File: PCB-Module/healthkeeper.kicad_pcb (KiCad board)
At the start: 2 copper layers, 85 x 76.8 mm, 28 parts, among them J1 RPI Conn, J2 24VDC-IN, J3 CTRL VALVE, J4 BAT Sense, J5 7"LCD Screen, J6 Flow Conn, J7 DpFlow Selector, Q1 IRF540NLPBF, U1 MCP4921-EP, U2 MCP6241, U3 TEN20-2411WIN, U4 MCP3208, U5 HSCSAAN001PDAA5, U6 HSCSAAN001PDAA5, U7 SDP816-125Pa

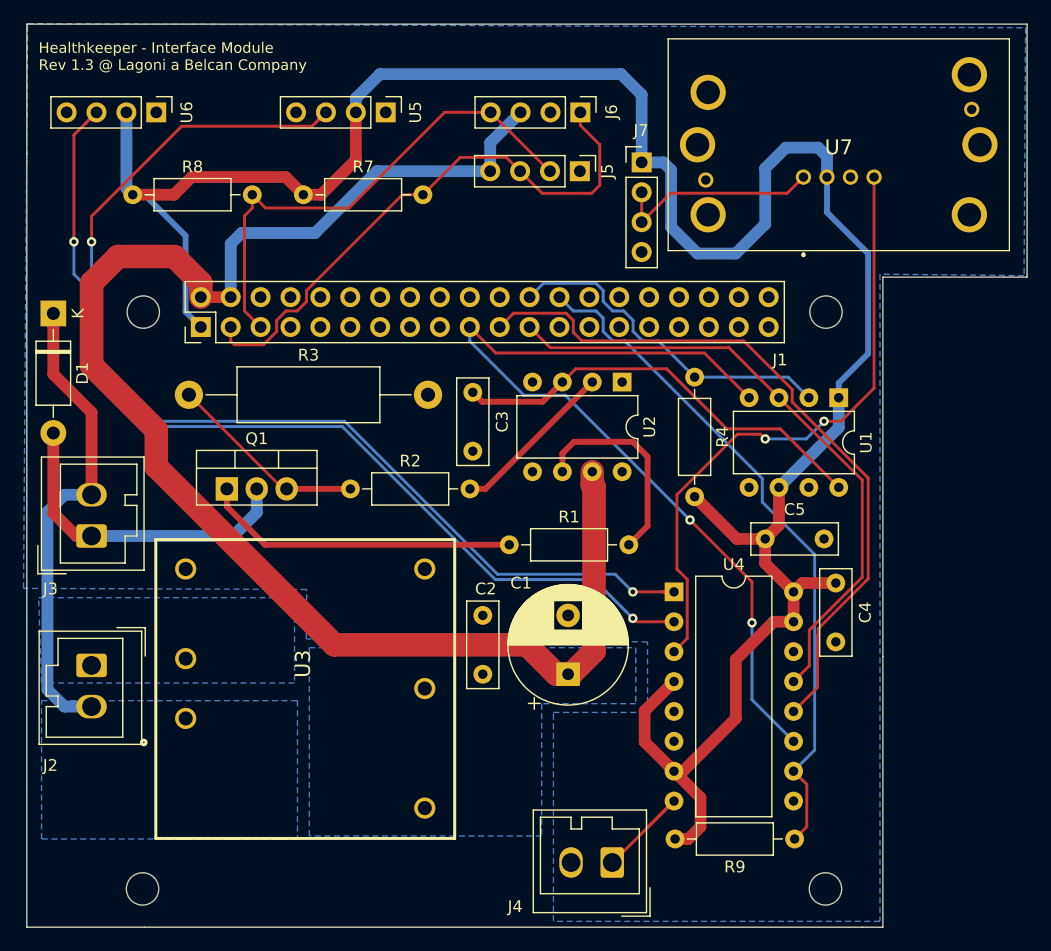
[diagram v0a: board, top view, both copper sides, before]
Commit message: Joint 24V and 5V ground
Error in the Rev 1.3 design as the 24V and 5V power weren't connected. This leads to an issue with the valve control.
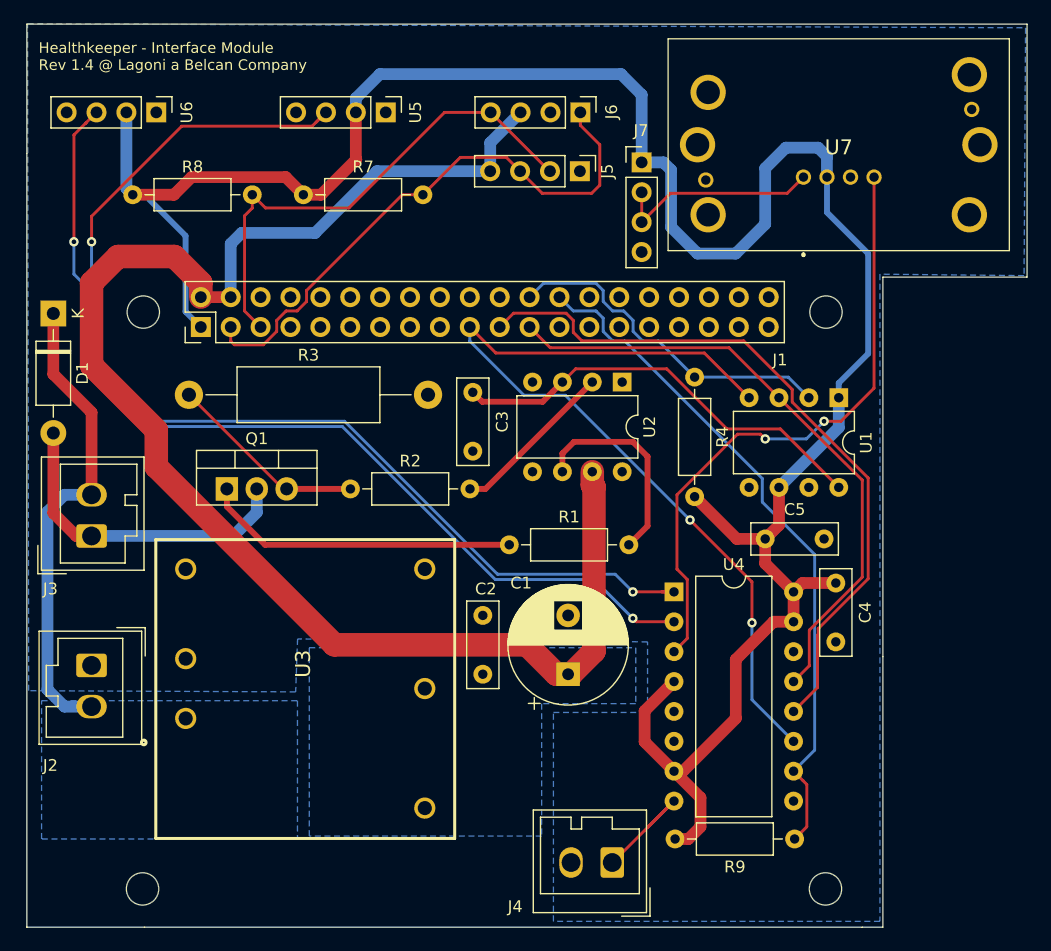
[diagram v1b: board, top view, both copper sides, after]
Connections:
- J2 pad 1: -24V -> GND
- U3 pad 2: -24V -> GND
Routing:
- removed copper zone on B.Cu, net -24V
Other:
- board text added: "Healthkeeper - Interface Module Rev 1.4 @ Lagoni a Belcan Company"
- board text removed: "Healthkeeper - Interface Module Rev 1.3 @ Lagoni a Belcan Company"

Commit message: Added RaspberryPI to the Footprint library
Added RaspberryPI to the Footprint library
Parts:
- J1: footprint Module:Raspberry_Pi4 -> Raspberry_Pi4:Raspberry_Pi4
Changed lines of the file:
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@@
     (add_net SPI_CS2)
   )
-  (module Module:Raspberry_Pi4 (layer F.Cu)
+  (module Raspberry_Pi4:Raspberry_Pi4 (layer F.Cu)
     (at 112.285859 71.865787 90)
     (descr "Raspberry Pi Zero using through hole straight pin socket, 2x20, 2.54mm pitch, https://www.raspberrypi.org/documentation/hardware/raspberrypi/mechanical/rpi_MECH_Zero_1p2.pdf")
